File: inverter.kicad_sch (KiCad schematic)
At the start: 20 parts, among them Q1 AON7264E-HXY, Q2 AON7264E-HXY, Q3 AON7264E-HXY, Q4 AON7264E-HXY, Q5 AON7264E-HXY, Q6 AON7264E-HXY

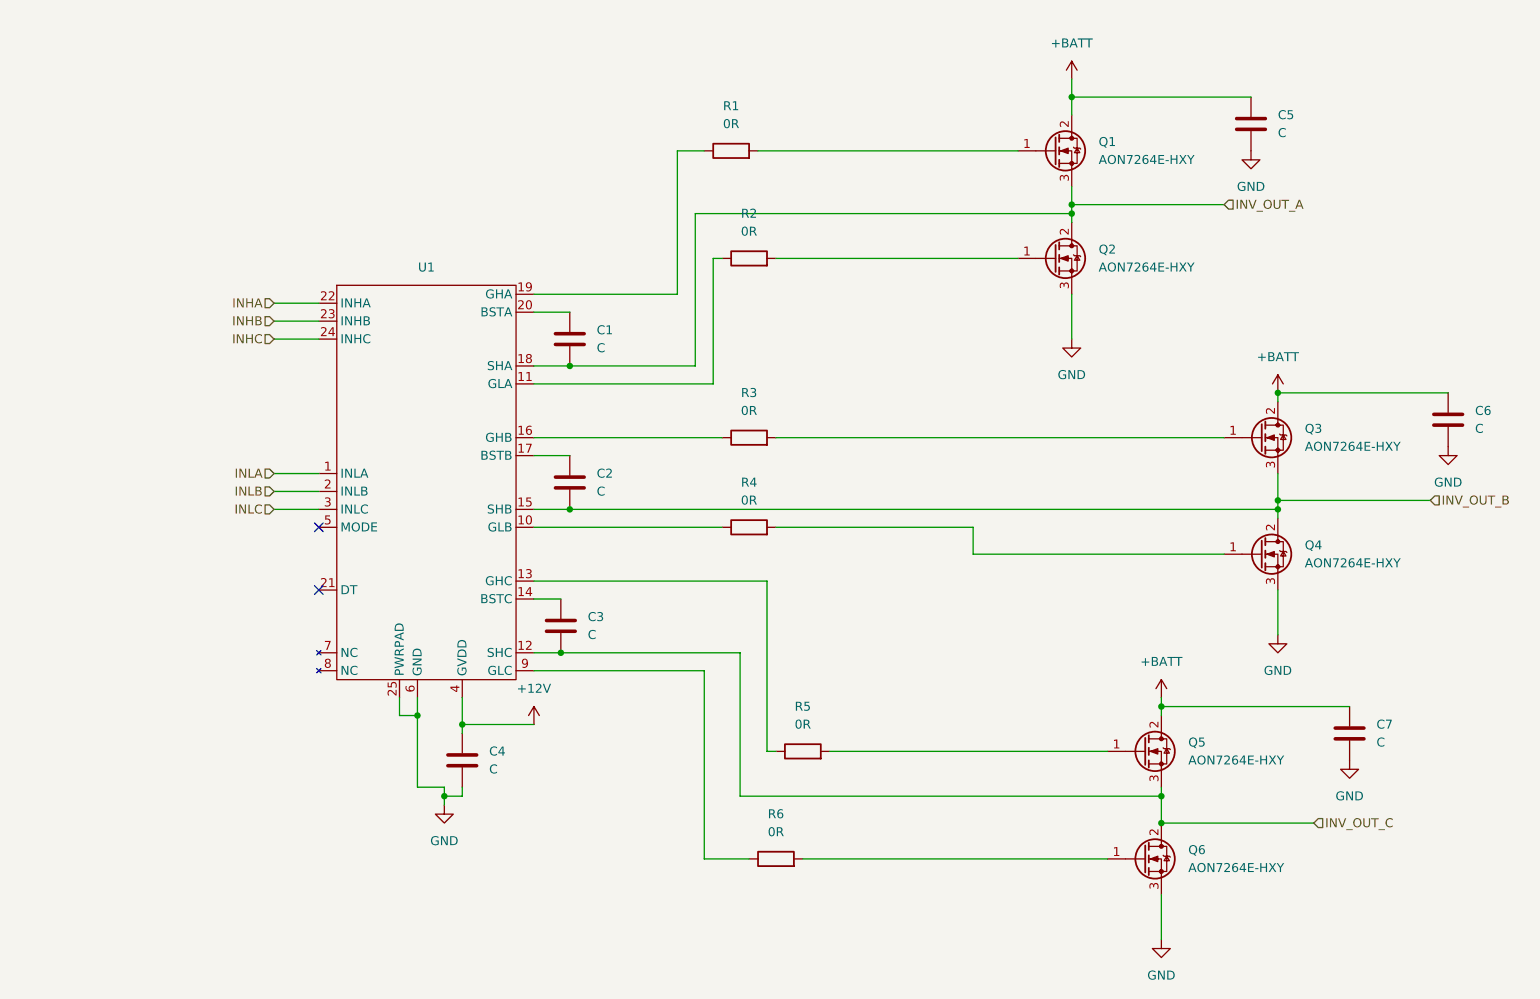
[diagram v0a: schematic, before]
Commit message: found real parts for capacitors, added 0 ohm resistors, added diode footprints for src line
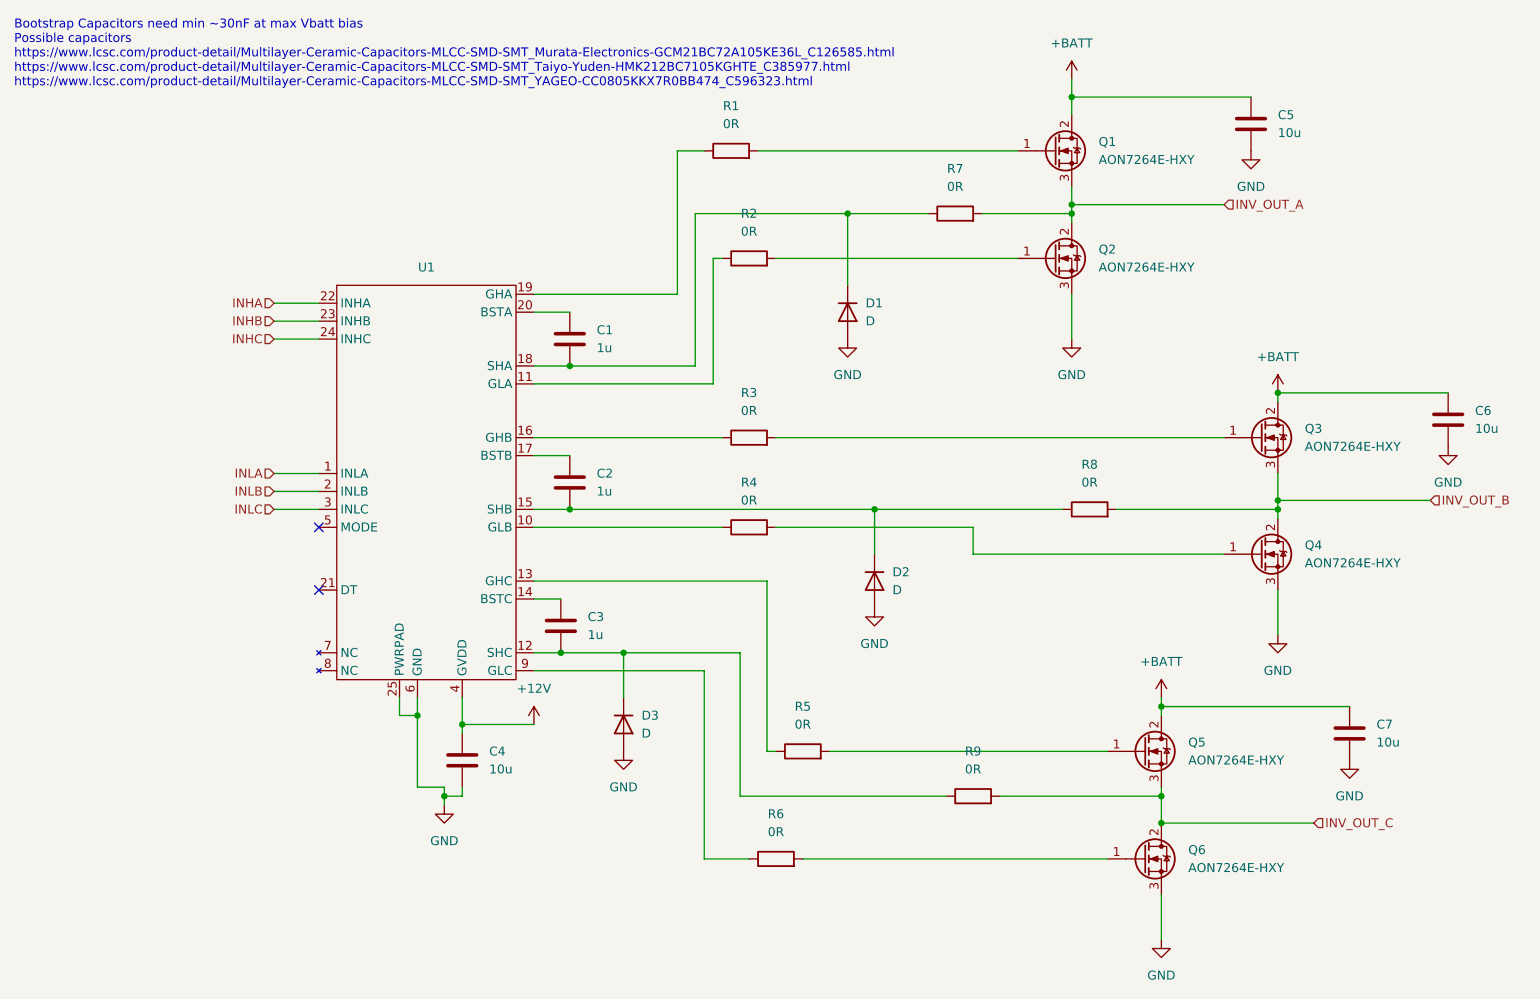
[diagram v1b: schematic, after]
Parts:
- added D1, D2, D3: D, Diode_SMD:D_0603_1608Metric, symbol Device:D
- added R7, R8, R9: 0R, Resistor_SMD:R_0402_1005Metric, symbol Device:R
- C1, C2, C3: value C -> 1u; footprint Capacitor_SMD:C_0402_1005Metric -> Capacitor_SMD:C_0805_2012Metric
- C4: value C -> 10u; footprint Capacitor_SMD:C_0603_1608Metric -> Capacitor_SMD:C_0805_2012Metric
- C5, C6, C7: value C -> 10u
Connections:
- net GND: now also D1.2 (A), D2.2 (A), D3.2 (A)
- net INV_OUT_A: now also R7.2; no longer C1.2, U1.18 (SHA)
- net INV_OUT_B: now also R8.2; no longer C2.2, U1.15 (SHB)
- net INV_OUT_C: now also R9.2; no longer C3.2, U1.12 (SHC)
- new net: C1.2, D1.1 (K), R7.1, U1.18 (SHA)
- new net: C3.2, D3.1 (K), R9.1, U1.12 (SHC)
- new net: C2.2, D2.1 (K), R8.1, U1.15 (SHB)
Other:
- note added: "Bootstrap Capacitors need min ~30nF at max Vbatt bias Possible capacitors https://www.lcsc.com/product-detail/Multilayer-Ceramic-Capacitors-MLCC-SMD-SMT_Murata-Electronics-GCM21BC72A105KE36L_C126585.html https://www.lcsc.com/product-detail/Multilayer-Ceramic-Capacitors-MLCC-SMD-SMT_Taiyo-Yuden-HMK212BC7105KGHTE_C385977.html https://www.lcsc.com/product-detail/Multilayer-Ceramic-Capacitors-MLCC-SM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"
